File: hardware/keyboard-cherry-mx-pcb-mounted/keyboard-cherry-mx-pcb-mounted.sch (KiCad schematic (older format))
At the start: 15 parts, among them J2 SWDConn, SW1 RST, U1 STM32F413RHTx, Y1 8MHz

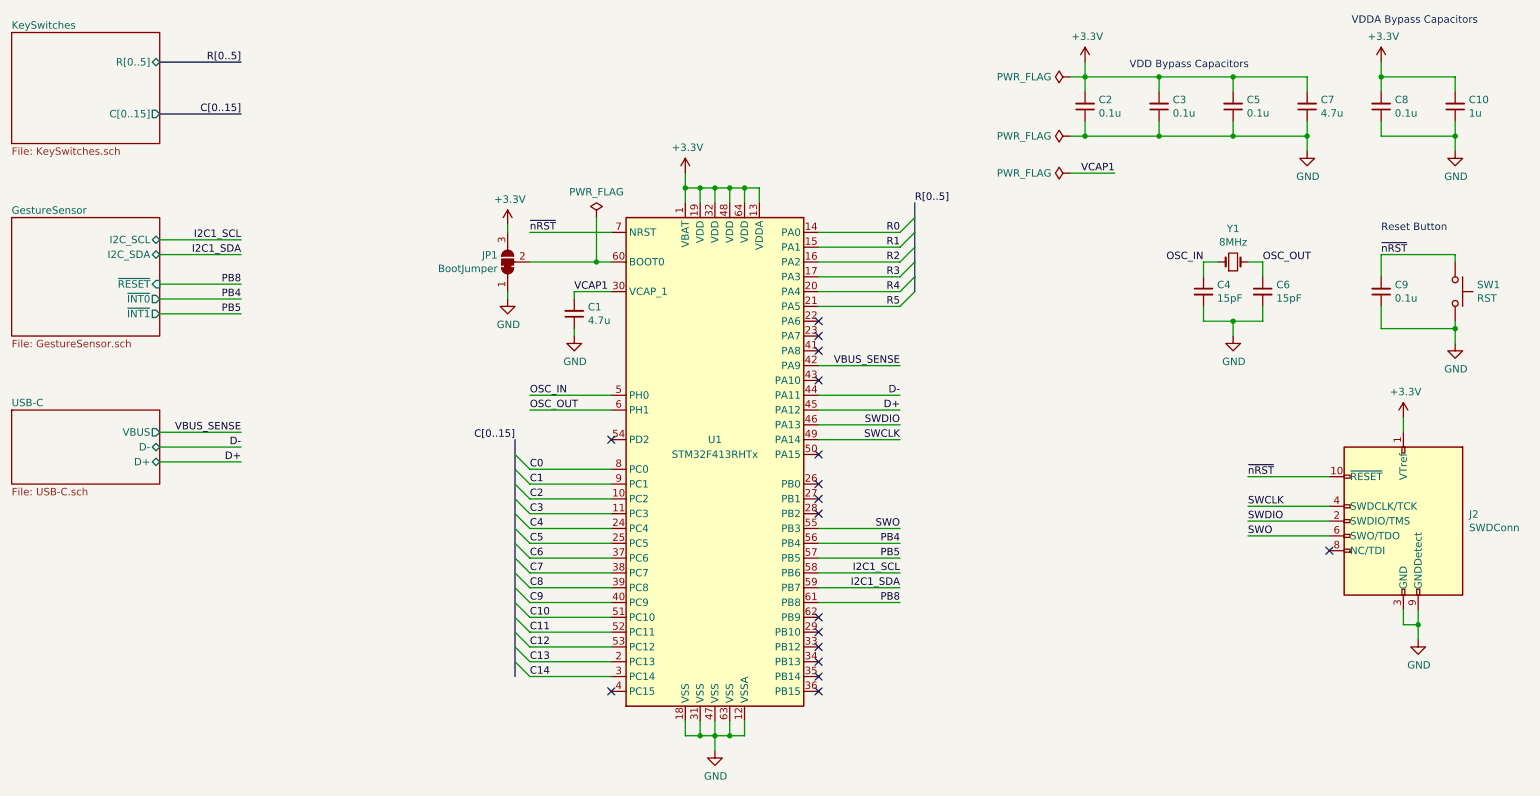
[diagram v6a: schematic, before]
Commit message: Adds more gesture sensors to the cherry mx pcb mounted keyboard.
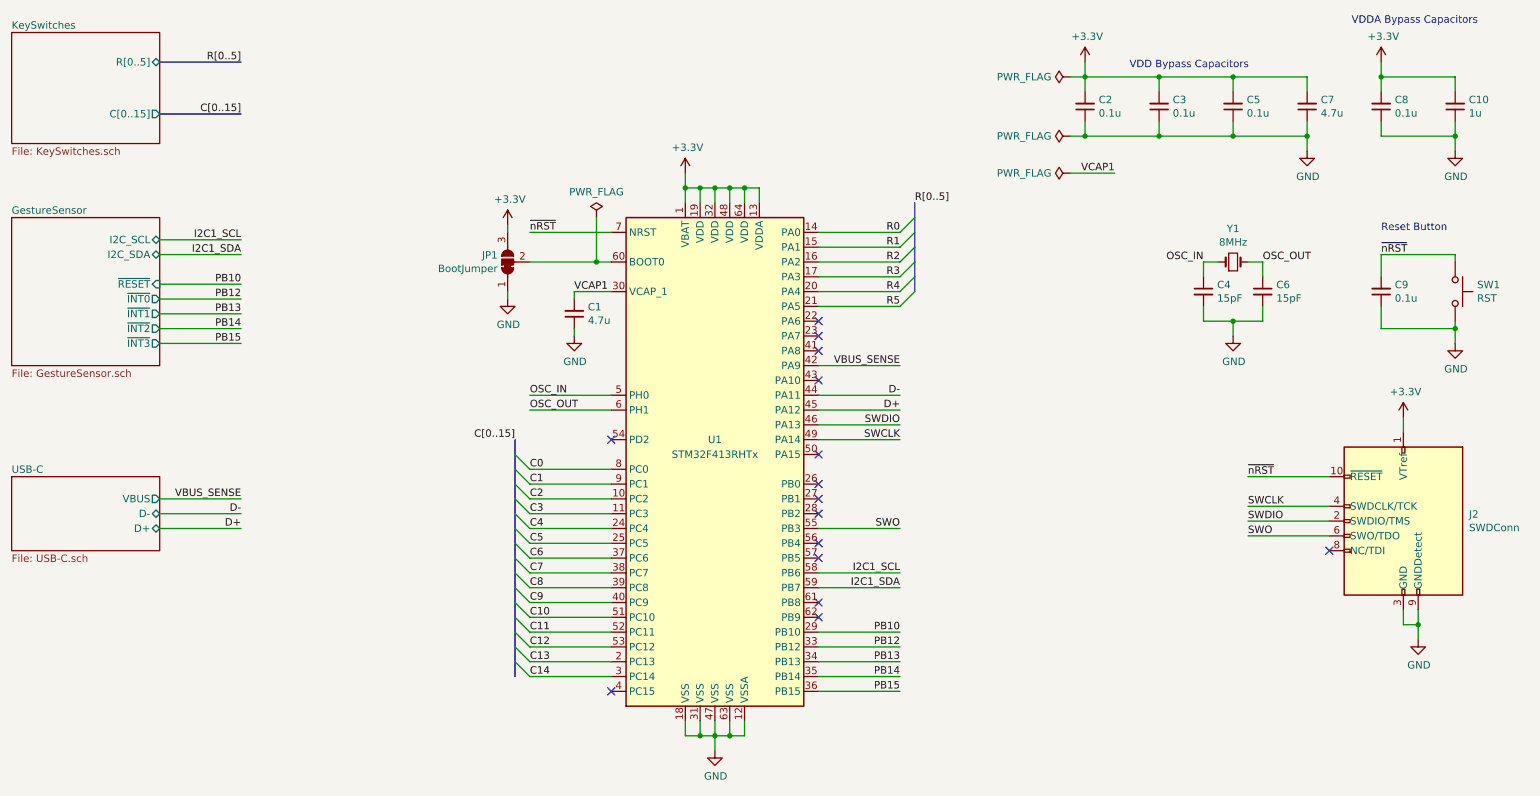
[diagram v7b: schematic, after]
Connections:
- net PB10: now reaches U1.29 (PB10)
- net PB12: now reaches U1.33 (PB12)
- net PB13: now reaches U1.34 (PB13)
- net PB14: now reaches U1.35 (PB14)
- net PB15: now reaches U1.36 (PB15)
- net PB4: no longer names the net of U1.56 (PB4)
- net PB5: no longer names the net of U1.57 (PB5)
- net PB8: no longer names the net of U1.61 (PB8)
- no-connect marks 17 -> 15
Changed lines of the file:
@@
 	4400 5250 4500 5350
 $Sheet
-S 1000 2250 1000 800
+S 1000 2250 1000 1000
 U 5E8711BD
 F0 "GestureSensor" 50
@@
 F5 "~INT0" O R 2000 2800 50
 F6 "~INT1" O R 2000 2900 50
+F7 "~INT2" O R 2000 3000 50
+F8 "~INT3" O R 2000 3100 50
 $EndSheet
-Text Label 2550 3700 2    50   ~ 0
+Text Label 2550 4150 2    50   ~ 0
 VBUS_SENSE
 Wire Wire Line
-	2000 3700 2550 3700
-Text Label 2550 3900 2    50   ~ 0
+	2000 4150 2550 4150
+Text Label 2550 4350 2    50   ~ 0
 D+
-Text Label 2550 3800 2    50   ~ 0
+Text Label 2550 4250 2    50   ~ 0
 D-
 Wire Wire Line
-	2000 3800 2550 3800
-Wire Wire Line
-	2000 3900 2550 3900
+	2000 4250 2550 4250
+Wire Wire Line
+	2000 4350 2550 4350
 $Sheet
-S 1000 3550 1000 500
+S 1000 4000 1000 500
 U 5E7D269A
 F0 "USB-C" 50
 F1 "USB-C.sch" 50
-F2 "D-" B R 2000 3800 50
-F3 "D+" B R 2000 3900 50
-F4 "VBUS" O R 2000 3700 50
+F2 "D-" B R 2000 4250 50
+F3 "D+" B R 2000 4350 50
+F4 "VBUS" O R 2000 4150 50
 $EndSheet
 Text Label 2550 2500 2    50   ~ 0
@@
 Wire Wire Line
 	10500 5000 10500 4900
-Text Label 2550 2700 2    50   ~ 0
-PB8
-Text Label 2550 2800 2    50   ~ 0
-PB4
-Text Label 2550 2900 2    50   ~ 0
-PB5
-Wire Wire Line
-	2000 2900 2550 2900
-Wire Wire Line
-	2550 2800 2000 2800
-Wire Wire Line
-	2000 2700 2550 2700
-Text Label 7000 4850 2    50   ~ 0
-PB8
-Text Label 7000 4450 2    50   ~ 0
-PB4
-Text Label 7000 4550 2    50   ~ 0
-PB5
-Wire Wire Line
-	6450 4550 7000 4550
-Wire Wire Line
-	7000 4450 6450 4450
-Wire Wire Line
-	6450 4850 7000 4850
+Text Label 7000 5050 2    50   ~ 0
+PB10
+Text Label 7000 5150 2    50   ~ 0
+PB12
+Text Label 7000 5250 2    50   ~ 0
+PB13
+Wire Wire Line
+	6450 5250 7000 5250
+Wire Wire Line
+	7000 5150 6450 5150
+Wire Wire Line
+	6450 5050 7000 5050
 Wire Wire Line
 	6450 4350 7000 4350
@@
 	8150 1700 8250 1700
 Connection ~ 8250 1700
-NoConn ~ 6450 4950
-NoConn ~ 6450 5050
-NoConn ~ 6450 5150
-NoConn ~ 6450 5250
-NoConn ~ 6450 5350
-NoConn ~ 6450 5450
 NoConn ~ 6450 4250
 NoConn ~ 6450 4150
@@
 Wire Wire Line
 	8150 1300 8250 1300
+Text Label 7000 5350 2    50   ~ 0
+PB14
+Text Label 7000 5450 2    50   ~ 0
+PB15
+Wire Wire Line
+	6450 5450 7000 5450
+Wire Wire Line
+	7000 5350 6450 5350
+NoConn ~ 6450 4850
+NoConn ~ 6450 4950
+NoConn ~ 6450 4450
+NoConn ~ 6450 4550
+Text Label 2550 2700 2    50   ~ 0
+PB10
+Text Label 2550 2800 2    50   ~ 0
+PB12
+Text Label 2550 2900 2    50   ~ 0
+PB13
+Wire Wire Line
+	2000 2900 2550 2900
+Wire Wire Line
+	2550 2800 2000 2800
+Wire Wire Line
+	2000 2700 2550 2700
+Text Label 2550 3000 2    50   ~ 0
+PB14
+Text Label 2550 3100 2    50   ~ 0
+PB15
+Wire Wire Line
+	2000 3100 2550 3100
+Wire Wire Line
+	2550 3000 2000 3000
 Wire Bus Line
 	7100 2150 7100 2750

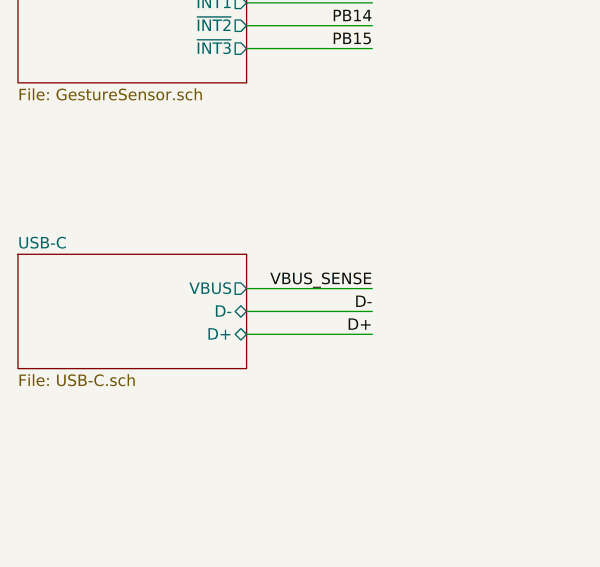
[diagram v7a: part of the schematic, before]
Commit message: Places diodes at respective locations on cherry mx pcb mounted keyboard.
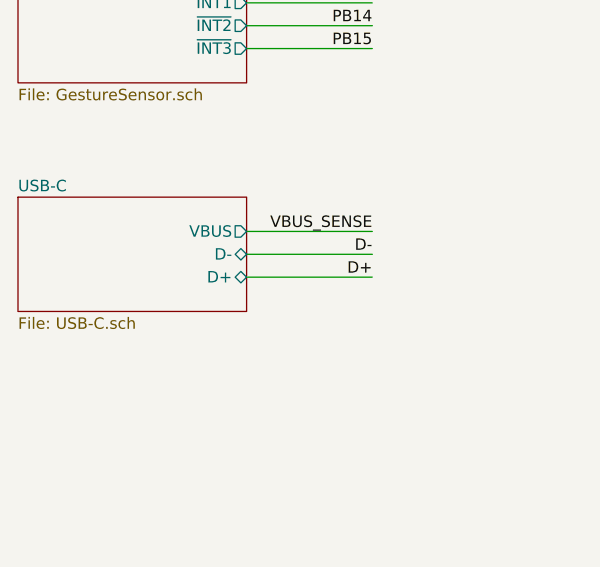
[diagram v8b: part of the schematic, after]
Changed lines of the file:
@@
 F8 "~INT3" O R 2000 3100 50
 $EndSheet
-Text Label 2550 4150 2    50   ~ 0
+Text Label 2550 3900 2    50   ~ 0
 VBUS_SENSE
 Wire Wire Line
-	2000 4150 2550 4150
-Text Label 2550 4350 2    50   ~ 0
+	2000 3900 2550 3900
+Text Label 2550 4100 2    50   ~ 0
 D+
-Text Label 2550 4250 2    50   ~ 0
+Text Label 2550 4000 2    50   ~ 0
 D-
 Wire Wire Line
-	2000 4250 2550 4250
+	2000 4000 2550 4000
 Wire Wire Line
-	2000 4350 2550 4350
+	2000 4100 2550 4100
 $Sheet
-S 1000 4000 1000 500
+S 1000 3750 1000 500
 U 5E7D269A
 F0 "USB-C" 50
 F1 "USB-C.sch" 50
-F2 "D-" B R 2000 4250 50
-F3 "D+" B R 2000 4350 50
-F4 "VBUS" O R 2000 4150 50
+F2 "D-" B R 2000 4000 50
+F3 "D+" B R 2000 4100 50
+F4 "VBUS" O R 2000 3900 50
 $EndSheet
 Text Label 2550 2500 2    50   ~ 0
